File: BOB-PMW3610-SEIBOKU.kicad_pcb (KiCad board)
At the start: 2 copper layers, 30 x 20 mm, 17 parts, among them J1 Conn_02x04_Odd_Even, U1 TLV70019DDCR, U2 PMW3610DM-SUDU

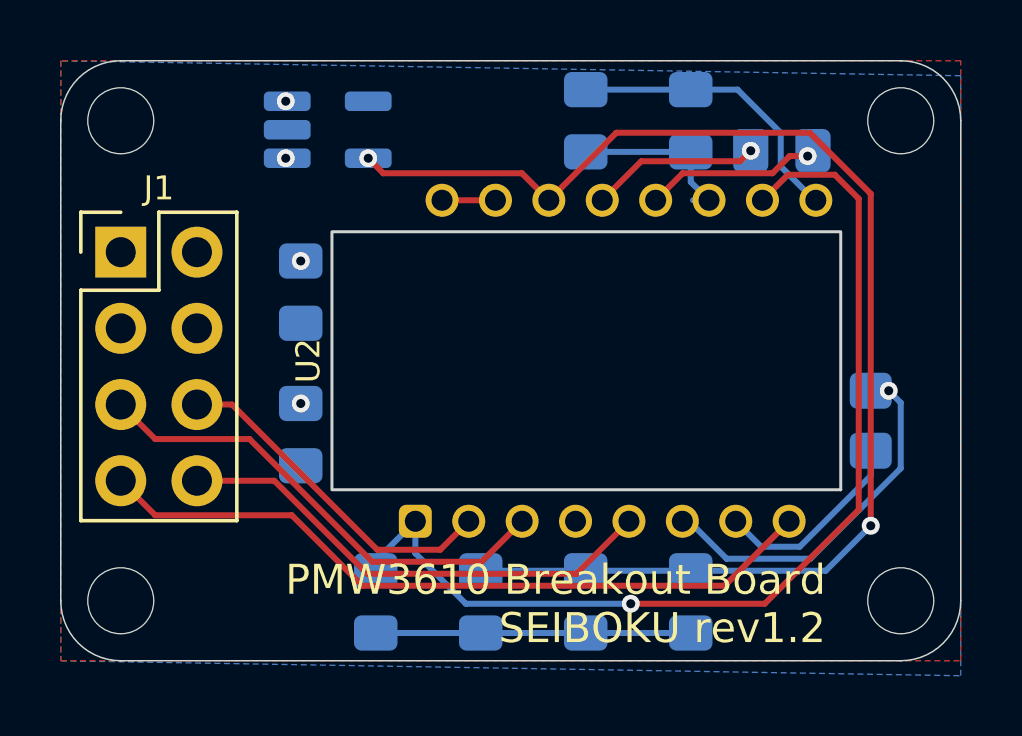
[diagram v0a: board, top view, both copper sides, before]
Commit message: Rev 1.3: 基板レイアウトの改善
- スティッチングビアを追加
- コンデンサの配置を変更
- シルクスクリーン位置を変更
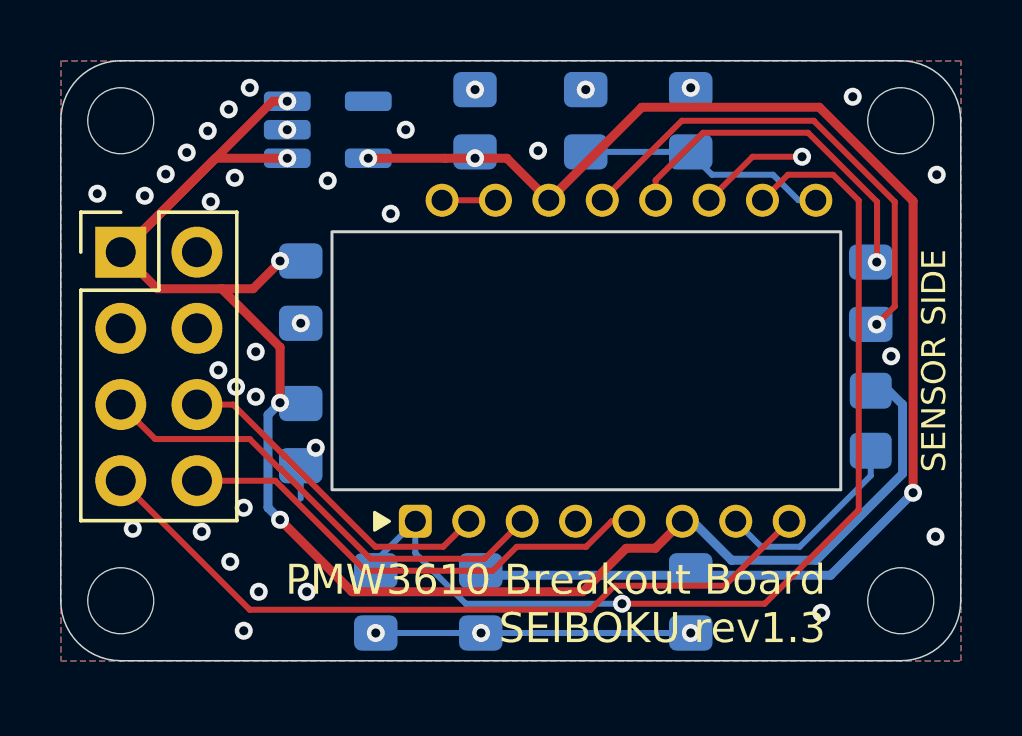
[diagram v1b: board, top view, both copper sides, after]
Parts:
- moved C2 16.5 mm to (146.5, 88.5), turned to 90 degrees
- moved C7 5.60 mm to (159.7, 94.2), turned to 90 degrees
- turned C5 to 90 degrees
- turned C8 to 90 degrees
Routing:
- net +3V3: track 11.8 -> 56.5 mm
- net Net-(U2-CN): track 5.63 -> 16.3 mm
- net Net-(U2-CP): track 5.68 -> 11.7 mm
- net +1V9: track 43.8 -> 46.8 mm, vias 2 -> 3
- net Net-(U2-VCP): track 9.85 -> 8.34 mm
- net GND: track 16.4 -> 15.3 mm, vias 0 -> 39
- net MOT: track 24.6 -> 25.3 mm
- added copper zone on F.Cu, net GND
- removed copper zone on F.Cu, net +3V3
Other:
- board text added: "LENDS SIDE"
- board text added: "PMW3610 Breakout Board SEIBOKU rev1.3"
- board text added: "SENSOR SIDE"
- board text removed: "LENDS"
- board text removed: "PMW3610 Breakout Board SEIBOKU rev1.2"
